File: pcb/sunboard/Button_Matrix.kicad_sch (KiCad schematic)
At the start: 154 parts

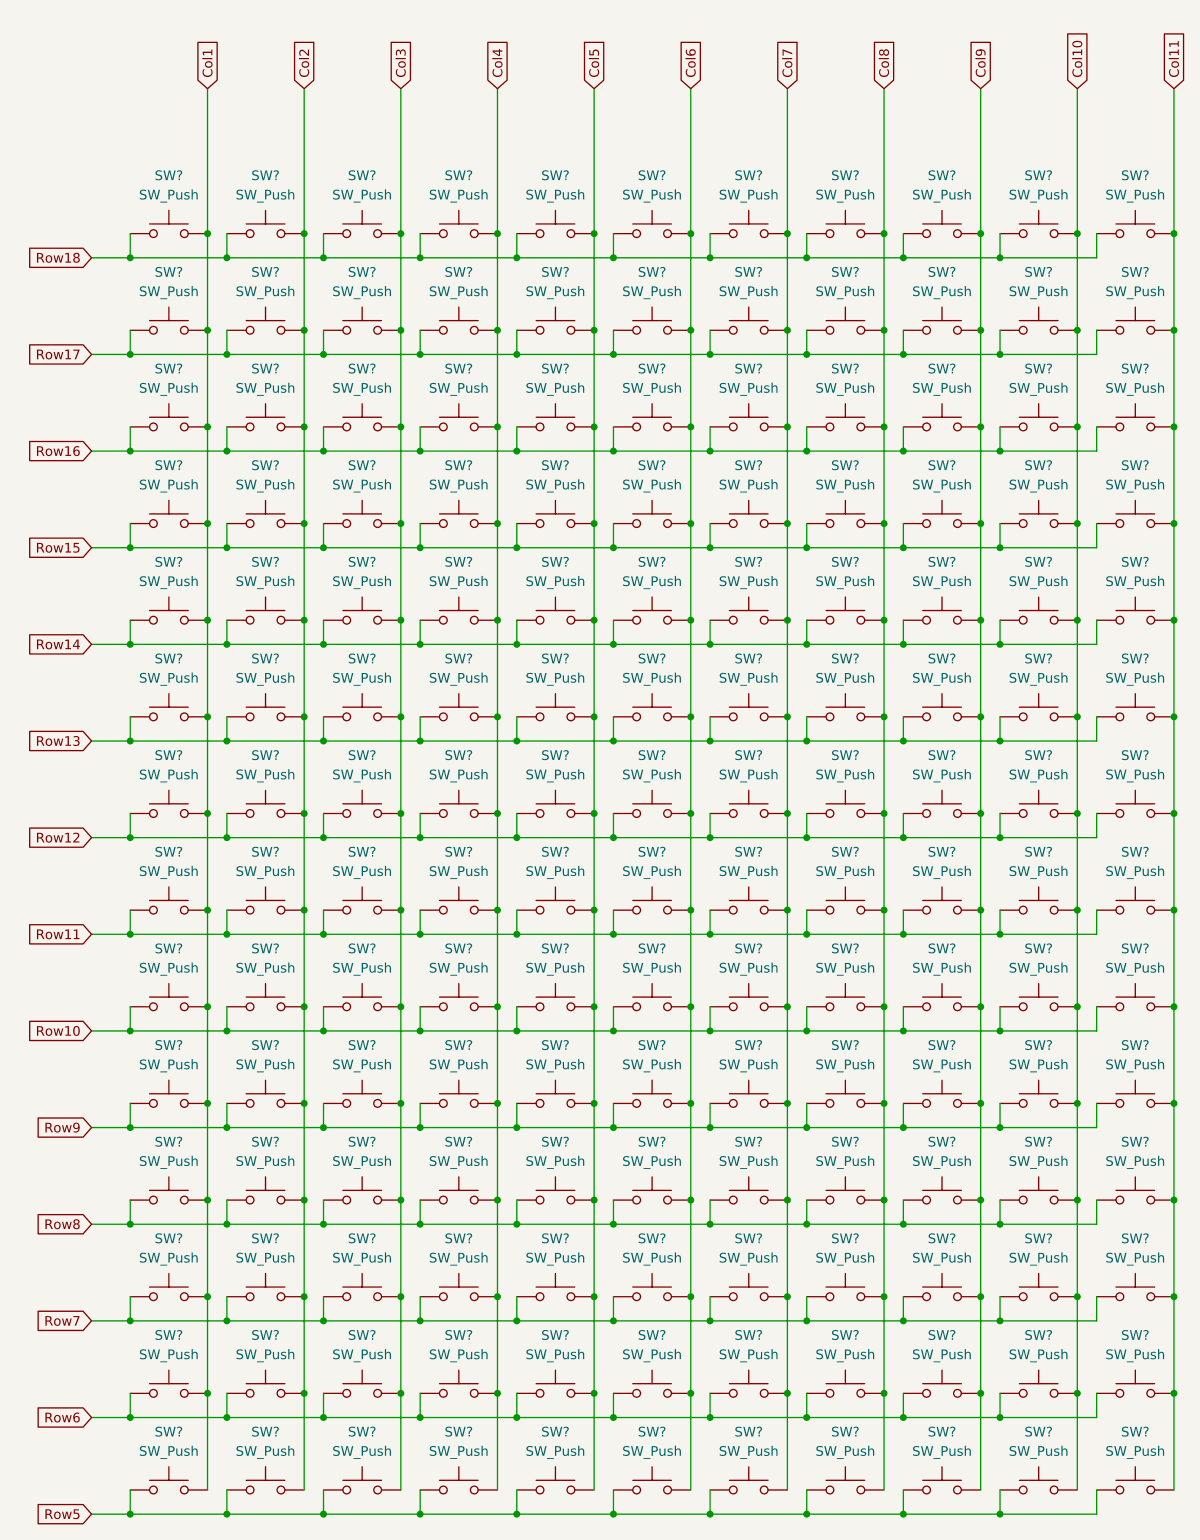
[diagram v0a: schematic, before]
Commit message: feat(pcb): add led driver
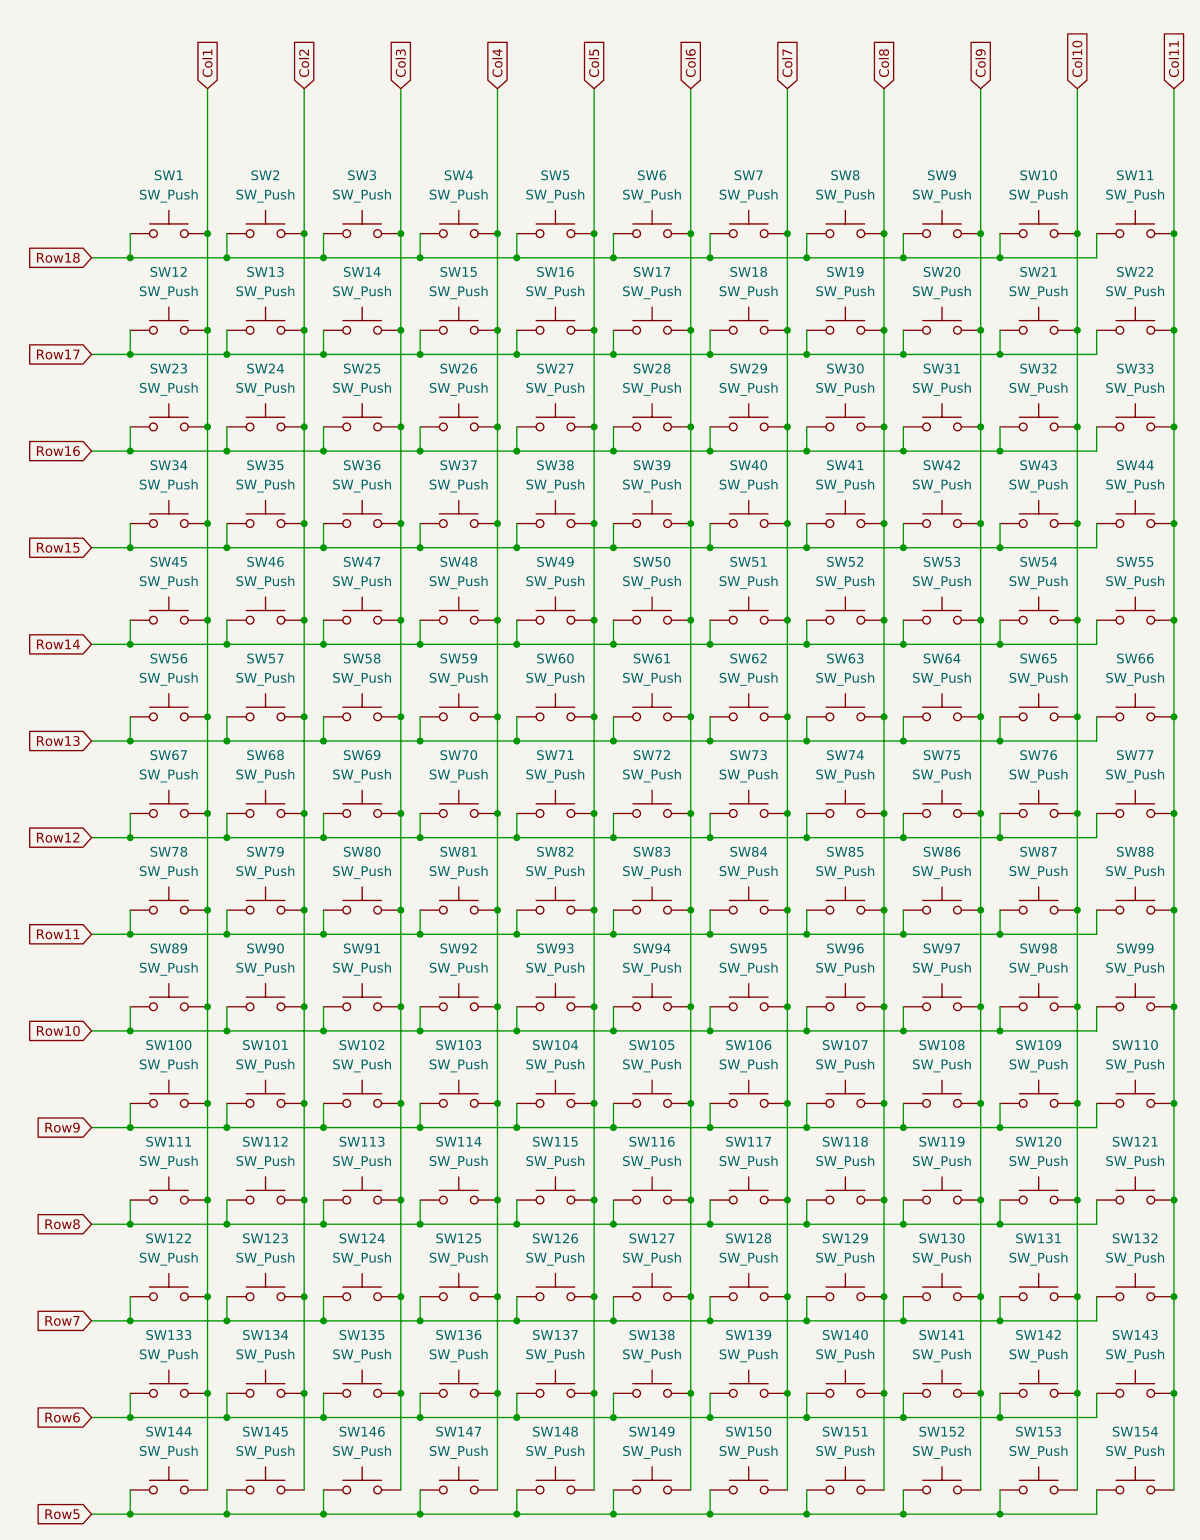
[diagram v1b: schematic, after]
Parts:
- gave numbers to parts that had none: 154

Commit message: feat(pcb): update schematic to use 6x6 buttons
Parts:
- SW1, SW10, SW100, SW101, SW102, SW103, SW104, SW105, SW106, SW107, SW108, SW109, SW11, SW110, SW111, SW112, SW113, SW114, SW115, SW116, SW117, SW118, SW119, SW12, SW120, SW121, SW122, SW123, SW124, SW125, SW126, SW127, SW128, SW129, SW13, SW130, SW131, SW132, SW133, SW134, SW135, SW136, SW137, SW138, SW139, SW14, SW140, SW141, SW142, SW143, SW144, SW145, SW146, SW147, SW148, SW149, SW15, SW150, SW151, SW152, SW153, SW154, SW16, SW17, SW18, SW19, SW2, SW20, SW21, SW22, SW23, SW24, SW25, SW26, SW27, SW28, SW29, SW3, SW30, SW31, SW32, SW33, SW34, SW35, SW36, SW37, SW38, SW39, SW4, SW40, SW41, SW42, SW43, SW44, SW45, SW46, SW47, SW48, SW49, SW5, SW50, SW51, SW52, SW53, SW54, SW55, SW56, SW57, SW58, SW59, SW6, SW60, SW61, SW62, SW63, SW64, SW65, SW66, SW67, SW68, SW69, SW7, SW70, SW71, SW72, SW73, SW74, SW75, SW76, SW77, SW78, SW79, SW8, SW80, SW81, SW82, SW83, SW84, SW85, SW86, SW87, SW88, SW89, SW9, SW90, SW91, SW92, SW93, SW94, SW95, SW96, SW97, SW98, SW99: footprint Button_Switch_SMD:SW_Tactile_SPST_NO_Straight_CK_PTS636Sx25SMTRLFS -> Button_Switch_SMD:SW_Push_1P1T_NO_6x6mm_H9.5mm

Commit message: feat(pcb): add display
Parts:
- SW1, SW10, SW100, SW101, SW102, SW103, SW104, SW105, SW106, SW107, SW108, SW109, SW11, SW110, SW111, SW112, SW113, SW114, SW115, SW116, SW117, SW118, SW119, SW12, SW120, SW121, SW122, SW123, SW124, SW125, SW126, SW127, SW128, SW129, SW13, SW130, SW131, SW132, SW133, SW134, SW135, SW136, SW137, SW138, SW139, SW14, SW140, SW141, SW142, SW143, SW144, SW145, SW146, SW147, SW148, SW149, SW15, SW150, SW151, SW152, SW153, SW154, SW16, SW17, SW18, SW19, SW2, SW20, SW21, SW22, SW23, SW24, SW25, SW26, SW27, SW28, SW29, SW3, SW30, SW31, SW32, SW33, SW34, SW35, SW36, SW37, SW38, SW39, SW4, SW40, SW41, SW42, SW43, SW44, SW45, SW46, SW47, SW48, SW49, SW5, SW50, SW51, SW52, SW53, SW54, SW55, SW56, SW57, SW58, SW59, SW6, SW60, SW61, SW62, SW63, SW64, SW65, SW66, SW67, SW68, SW69, SW7, SW70, SW71, SW72, SW73, SW74, SW75, SW76, SW77, SW78, SW79, SW8, SW80, SW81, SW82, SW83, SW84, SW85, SW86, SW87, SW88, SW89, SW9, SW90, SW91, SW92, SW93, SW94, SW95, SW96, SW97, SW98, SW99: JLCPCB Part # (none) -> C455109
